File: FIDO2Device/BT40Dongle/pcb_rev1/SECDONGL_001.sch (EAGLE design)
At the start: 36 parts, among them CN1 CX60-24S-UNIT, CN2 IF_5PIN_H, CN3 IF_4PIN_SOL, SW1 SKRPACE010, SW2 SKRPACE010, SW3 SKTADAE010, U1 BT40, U2 ADP122ACPZ-3.3-R7, U3 RV-3028-C7

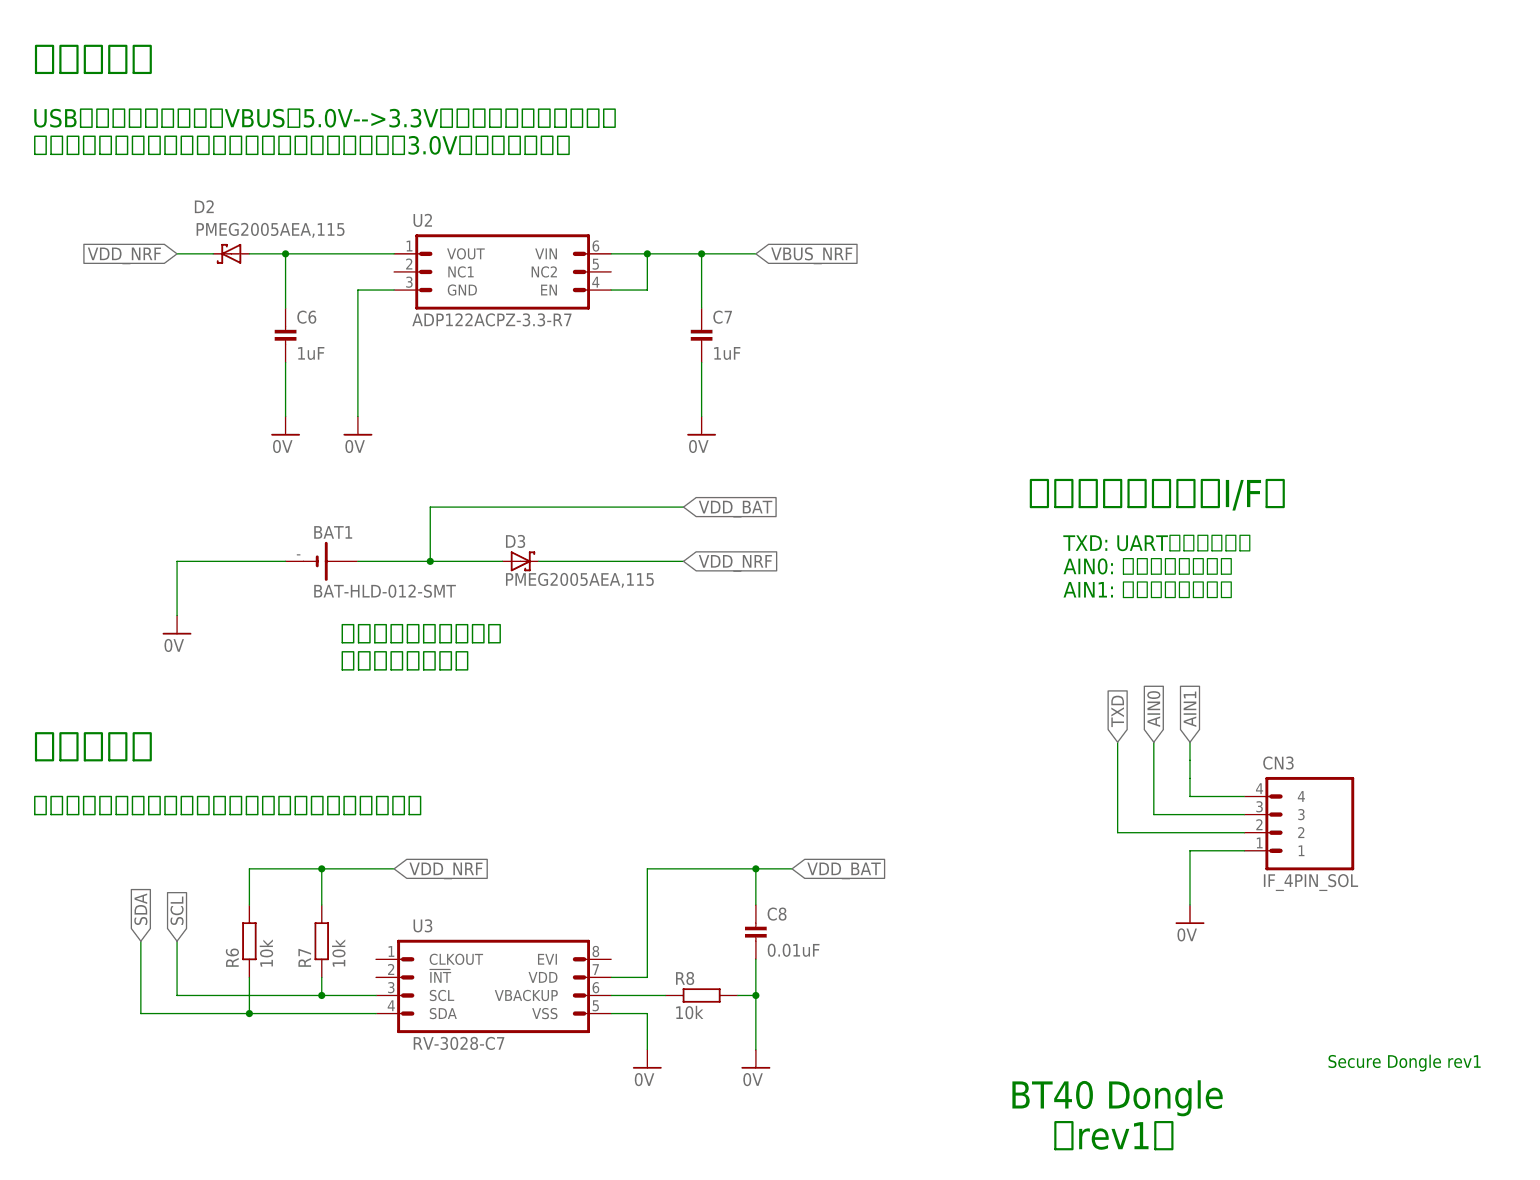
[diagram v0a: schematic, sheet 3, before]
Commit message: 回路図を修正
・指摘点の反映
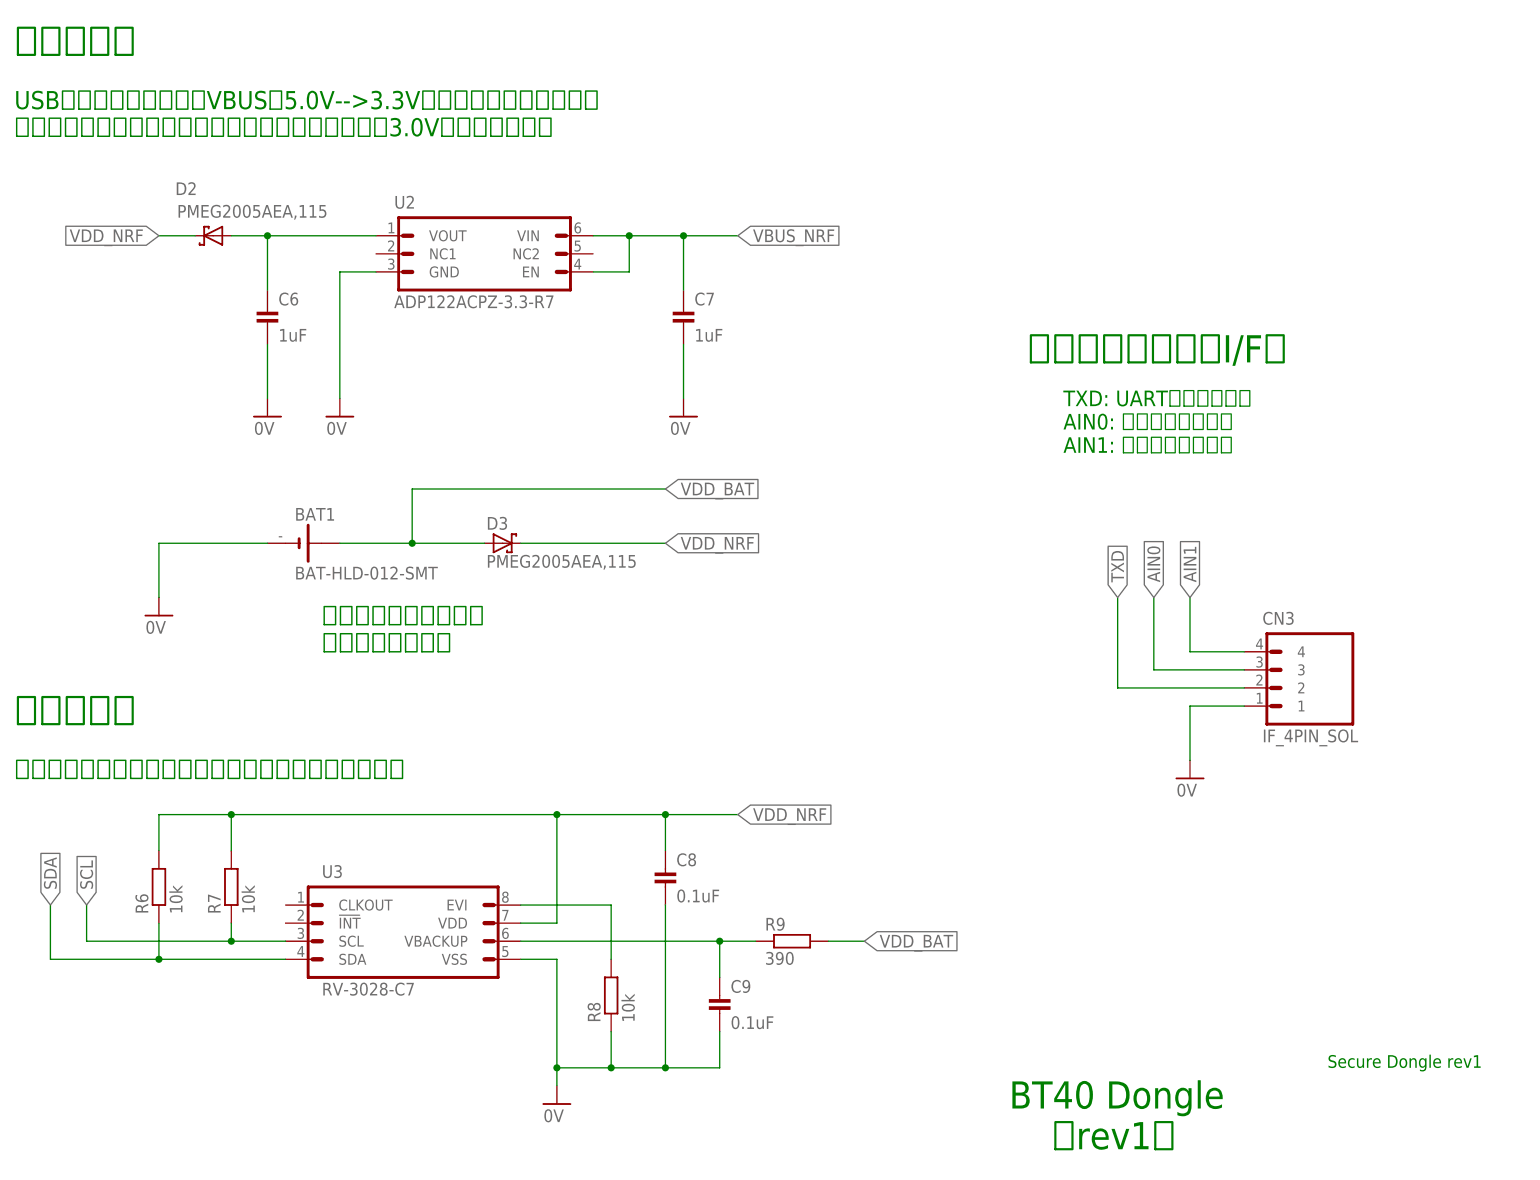
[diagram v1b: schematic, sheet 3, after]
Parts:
- added C9: 0.1uF, Parts:CAP_0402K
- added R9: 390, Parts:RESISTOR_0402
- C8: value 0.01uF -> 0.1uF
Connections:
- removed net N$10: R8.1, U3.VBACKUP
- new net N$4: C9.1, R9.1, U3.VBACKUP
- new net N$5: R8.2, U3.EVI
- net 0V: now also C9.2, R8.1; no longer R8.2
- net VDD_BAT: now also R9.2; no longer C8.1, U3.VDD
- net VDD_NRF: now also C8.1, U3.VDD
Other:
- moved on the sheet: BAT1, C6, C7, C8, CN3, D2, D3, R6, R7, R8, U2, U3

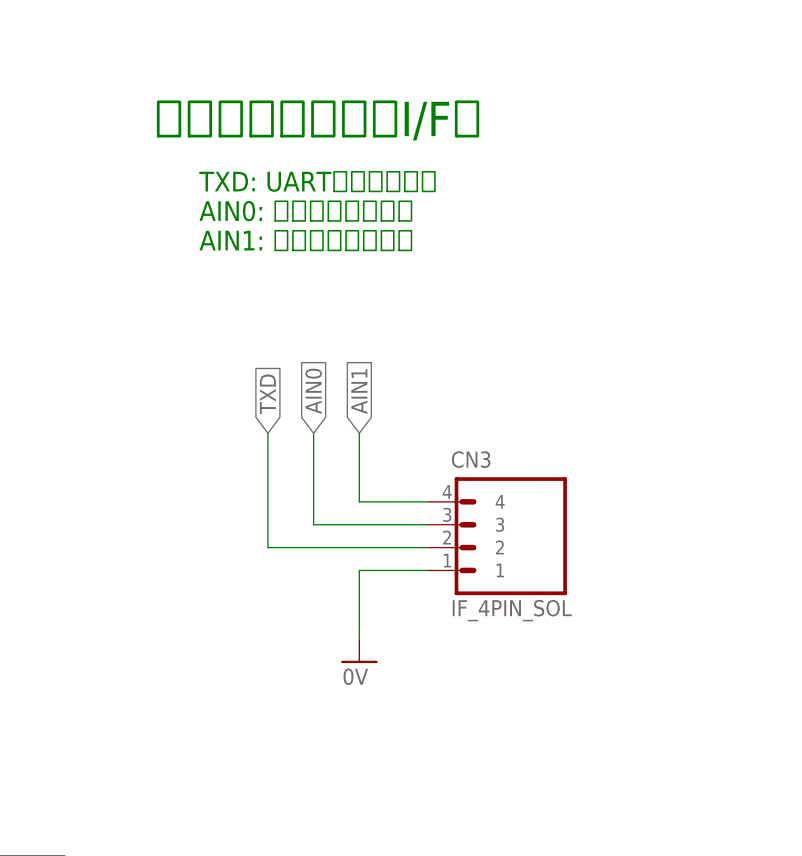
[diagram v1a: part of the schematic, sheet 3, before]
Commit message: 回路図を修正
・アナログ入力ピンを削除
（スペースの関係上、配置不可と判断）
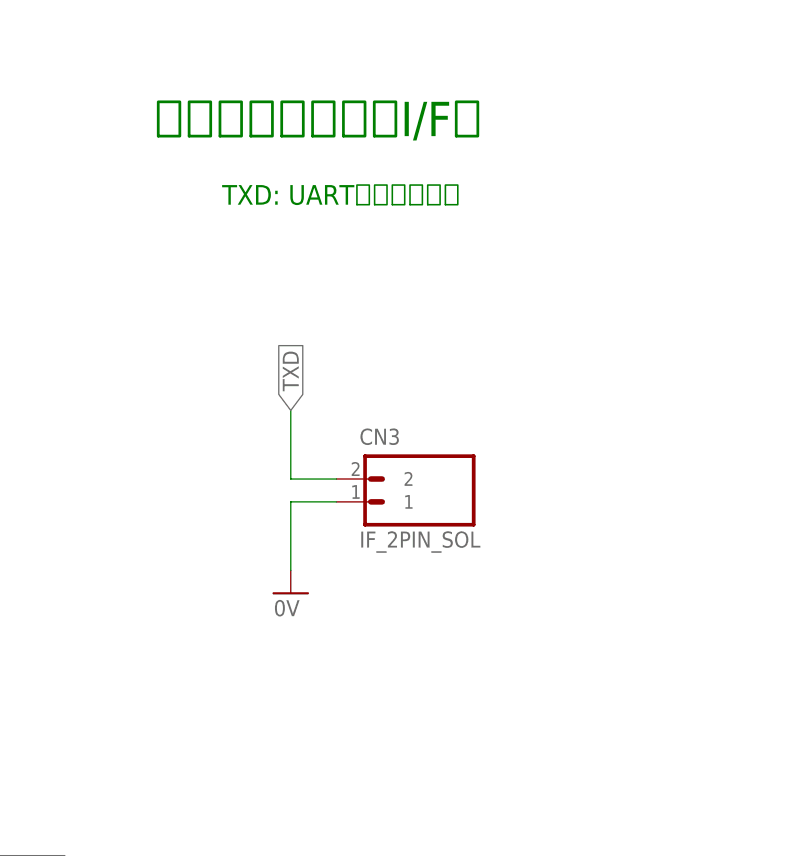
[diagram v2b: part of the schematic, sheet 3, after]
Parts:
- CN3: value IF_4PIN_SOL -> IF_2PIN_SOL; device Connectors:IF_4PIN_SOL -> Connectors:IF_2PIN_SOL
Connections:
- removed net AIN0: CN3.3, U1.P0.04/AIN0
- removed net AIN1: CN3.4, U1.P0.05/AIN1
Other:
- note added: "TXD: UARTデバッグ出力"
- note removed: "TXD: UARTデバッグ出力 AIN0: 基準電圧測定入力 AIN1: 電池電圧測定入力"
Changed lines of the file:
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@@
 <part name="CN2" library="Connectors" deviceset="IF_5PIN" device="_H"/>
 <part name="GND3" library="Supply" deviceset="0V" device=""/>
-<part name="CN3" library="Connectors" deviceset="IF_4PIN" device="_SOL"/>
 <part name="CN1" library="Connectors" deviceset="CX60-24S-UNIT" device=""/>
 <part name="U3" library="ICs" deviceset="RV-3028-C7" device=""/>
@@
 <part name="C9" library="Parts" deviceset="CAP" device="_0402K" value="0.1uF"/>
 <part name="R9" library="Parts" deviceset="RESISTOR" device="_0402" value="390"/>
+<part name="CN3" library="Connectors" deviceset="IF_2PIN" device="_SOL"/>
 </parts>
 <sheets>
@@
 <wire x1="106.68" y1="66.04" x2="88.9" y2="66.04" width="0.1524" layer="91"/>
 <label x="88.9" y="66.04" size="1.778" layer="95" rot="R180" xref="yes"/>
-</segment>
-</net>
-<net name="AIN0" class="0">
-<segment>
-<pinref part="U1" gate="G$1" pin="P0.04/AIN0"/>
-<wire x1="30.48" y1="121.92" x2="20.32" y2="121.92" width="0.1524" layer="91"/>
-<wire x1="20.32" y1="121.92" x2="20.32" y2="66.04" width="0.1524" layer="91"/>
-<wire x1="20.32" y1="66.04" x2="35.56" y2="66.04" width="0.1524" layer="91"/>
-<label x="35.56" y="66.04" size="1.778" layer="95" xref="yes"/>
-</segment>
-</net>
-<net name="AIN1" class="0">
-<segment>
-<pinref part="U1" gate="G$1" pin="P0.05/AIN1"/>
-<wire x1="30.48" y1="119.38" x2="22.86" y2="119.38" width="0.1524" layer="91"/>
-<wire x1="22.86" y1="119.38" x2="22.86" y2="71.12" width="0.1524" layer="91"/>
-<wire x1="22.86" y1="71.12" x2="35.56" y2="71.12" width="0.1524" layer="91"/>
-<label x="35.56" y="71.12" size="1.778" layer="95" xref="yes"/>
 </segment>
 </net>
@@
 基板の表面に実装</text>
 <text x="175.26" y="119.38" size="3.81" layer="91">ユーティリティーI/F部</text>
-<text x="180.34" y="106.68" size="2.1844" layer="91">TXD: UARTデバッグ出力
-AIN0: 基準電圧測定入力
-AIN1: 電池電圧測定入力</text>
+<text x="182.88" y="111.76" size="2.1844" layer="91">TXD: UARTデバッグ出力</text>
 <text x="217.424" y="20.32" size="1.778" layer="91">Secure Dongle rev1</text>
 <text x="172.72" y="8.89" size="3.81" layer="91">BT40 Dongle
@@
 <instance part="GND19" gate="1" x="53.34" y="83.82"/>
 <instance part="U2" gate="G$1" x="83.82" y="134.62"/>
-<instance part="GND3" gate="1" x="198.12" y="60.96"/>
-<instance part="CN3" gate="G$1" x="205.74" y="78.74"/>
+<instance part="GND3" gate="1" x="190.5" y="68.58"/>
 <instance part="U3" gate="G$1" x="73.66" y="40.64"/>
 <instance part="GND20" gate="1" x="109.22" y="15.24"/>
@@
 <instance part="C9" gate="G$1" x="132.08" y="33.02"/>
 <instance part="R9" gate="G$1" x="137.16" y="38.1"/>
+<instance part="CN3" gate="G$1" x="195.58" y="81.28"/>
 </instances>
 <busses>
@@
 </segment>
 <segment>
+<pinref part="GND3" gate="1" pin="0V"/>
+<wire x1="190.5" y1="78.74" x2="190.5" y2="71.12" width="0.1524" layer="91"/>
 <pinref part="CN3" gate="G$1" pin="1"/>
-<pinref part="GND3" gate="1" pin="0V"/>
-<wire x1="205.74" y1="71.12" x2="198.12" y2="71.12" width="0.1524" layer="91"/>
-<wire x1="198.12" y1="71.12" x2="198.12" y2="63.5" width="0.1524" layer="91"/>
+<wire x1="195.58" y1="78.74" x2="190.5" y2="78.74" width="0.1524" layer="91"/>
 </segment>
 <segment>
@@
 </segment>
 </net>
-<net name="AIN0" class="0">
-<segment>
-<wire x1="193.04" y1="76.2" x2="193.04" y2="86.36" width="0.1524" layer="91"/>
-<label x="193.04" y="86.36" size="1.778" layer="95" rot="R90" xref="yes"/>
-<pinref part="CN3" gate="G$1" pin="3"/>
-<wire x1="205.74" y1="76.2" x2="193.04" y2="76.2" width="0.1524" layer="91"/>
-</segment>
-</net>
 <net name="TXD" class="0">
 <segment>
-<wire x1="187.96" y1="73.66" x2="187.96" y2="86.36" width="0.1524" layer="91"/>
-<label x="187.96" y="86.36" size="1.778" layer="95" rot="R90" xref="yes"/>
+<wire x1="190.5" y1="81.28" x2="190.5" y2="88.9" width="0.1524" layer="91"/>
+<label x="190.5" y="88.9" size="1.778" layer="95" rot="R90" xref="yes"/>
 <pinref part="CN3" gate="G$1" pin="2"/>
-<wire x1="205.74" y1="73.66" x2="187.96" y2="73.66" width="0.1524" layer="91"/>
-</segment>
-</net>
-<net name="AIN1" class="0">
-<segment>
-<label x="198.12" y="86.36" size="1.778" layer="95" rot="R90" xref="yes"/>
-<pinref part="CN3" gate="G$1" pin="4"/>
-<wire x1="205.74" y1="78.74" x2="198.12" y2="78.74" width="0.1524" layer="91"/>
-<wire x1="198.12" y1="78.74" x2="198.12" y2="86.36" width="0.1524" layer="91"/>
-</segment>
-</net>
+<wire x1="195.58" y1="81.28" x2="190.5" y2="81.28" width="0.1524" layer="91"/>
+</segment>
+</net>

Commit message: 配線レイアウトの作成
・サイズを小型化（30mm x 20mm）するため、部品レイアウトを修正
・部品番号を変更（FBx --> Lx）
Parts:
- renumbered FB1 to L1, FB2 to L2, FB3 to L3
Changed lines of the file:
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@@
 <part name="FRAME2" library="Generic" deviceset="A4L-LOC" device=""/>
 <part name="FRAME3" library="Generic" deviceset="A4L-LOC" device=""/>
-<part name="FB1" library="Parts" deviceset="BLM15AG" device="121SN1D"/>
-<part name="FB2" library="Parts" deviceset="BLM15AG" device="121SN1D"/>
+<part name="L1" library="Parts" deviceset="BLM15AG" device="121SN1D"/>
+<part name="L2" library="Parts" deviceset="BLM15AG" device="121SN1D"/>
 <part name="C2" library="Parts" deviceset="CAP" device="_0402K" value="0.01uF"/>
 <part name="C5" library="Parts" deviceset="CAP" device="_0603" value="10uF"/>
@@
 <part name="GND10" library="Supply" deviceset="0V" device=""/>
 <part name="GND14" library="Supply" deviceset="0V" device=""/>
-<part name="FB3" library="Parts" deviceset="BLM15AG" device="121SN1D"/>
+<part name="L3" library="Parts" deviceset="BLM15AG" device="121SN1D"/>
 <part name="D1" library="Parts" deviceset="PRTR5V0U2X" device=""/>
 <part name="R3" library="Parts" deviceset="RESISTOR" device="_0402" value="1.2k"/>
@@
 <instances>
 <instance part="FRAME2" gate="G$1" x="0" y="0"/>
-<instance part="FB1" gate="G$1" x="121.92" y="154.94"/>
-<instance part="FB2" gate="G$1" x="121.92" y="121.92"/>
+<instance part="L1" gate="G$1" x="121.92" y="154.94"/>
+<instance part="L2" gate="G$1" x="121.92" y="121.92"/>
 <instance part="C2" gate="G$1" x="116.84" y="152.4"/>
 <instance part="C5" gate="G$1" x="226.06" y="124.46"/>
@@
 <instance part="GND10" gate="1" x="149.86" y="139.7"/>
 <instance part="GND14" gate="1" x="149.86" y="99.06"/>
-<instance part="FB3" gate="G$1" x="121.92" y="109.22"/>
+<instance part="L3" gate="G$1" x="121.92" y="109.22"/>
 <instance part="D1" gate="G$1" x="160.02" y="121.92"/>
 <instance part="R3" gate="G$1" x="68.58" y="33.02" rot="R90"/>
@@
 <segment>
 <wire x1="106.68" y1="134.62" x2="106.68" y2="139.7" width="0.1524" layer="91"/>
-<pinref part="FB1" gate="G$1" pin="1"/>
+<pinref part="L1" gate="G$1" pin="1"/>
 <wire x1="106.68" y1="139.7" x2="106.68" y2="154.94" width="0.1524" layer="91"/>
 <wire x1="106.68" y1="154.94" x2="116.84" y2="154.94" width="0.1524" layer="91"/>
@@
 <net name="VBUS_NRF" class="0">
 <segment>
-<pinref part="FB1" gate="G$1" pin="2"/>
+<pinref part="L1" gate="G$1" pin="2"/>
 <wire x1="139.7" y1="154.94" x2="149.86" y2="154.94" width="0.1524" layer="91"/>
 <pinref part="C3" gate="G$1" pin="1"/>
@@
 <segment>
 <pinref part="GND14" gate="1" pin="0V"/>
-<pinref part="FB2" gate="G$1" pin="2"/>
+<pinref part="L2" gate="G$1" pin="2"/>
 <wire x1="139.7" y1="121.92" x2="149.86" y2="121.92" width="0.1524" layer="91"/>
 <wire x1="149.86" y1="121.92" x2="149.86" y2="109.22" width="0.1524" layer="91"/>
 <junction x="149.86" y="109.22"/>
-<pinref part="FB3" gate="G$1" pin="2"/>
+<pinref part="L3" gate="G$1" pin="2"/>
 <wire x1="149.86" y1="109.22" x2="149.86" y2="101.6" width="0.1524" layer="91"/>
 <wire x1="139.7" y1="109.22" x2="149.86" y2="109.22" width="0.1524" layer="91"/>
@@
 <net name="USB_GND" class="0">
 <segment>
-<pinref part="FB2" gate="G$1" pin="1"/>
+<pinref part="L2" gate="G$1" pin="1"/>
 <wire x1="121.92" y1="121.92" x2="88.9" y2="121.92" width="0.1524" layer="91"/>
 <pinref part="R1" gate="G$1" pin="1"/>
@@
 <net name="FG" class="0">
 <segment>
-<pinref part="FB3" gate="G$1" pin="1"/>
+<pinref part="L3" gate="G$1" pin="1"/>
 <wire x1="81.28" y1="96.52" x2="81.28" y2="109.22" width="0.1524" layer="91"/>
 <wire x1="81.28" y1="109.22" x2="121.92" y2="109.22" width="0.1524" layer="91"/>
